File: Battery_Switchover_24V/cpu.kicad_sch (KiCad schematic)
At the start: 39 parts, among them J1 USB_C_Receptacle_USB2.0_14P, M1 Fan, Q1 PZT2222AT1G, SW1 SW_Push, U14 OPA2197xD, U3 LPC11U14FBD48-201, Y1 12.000MHz

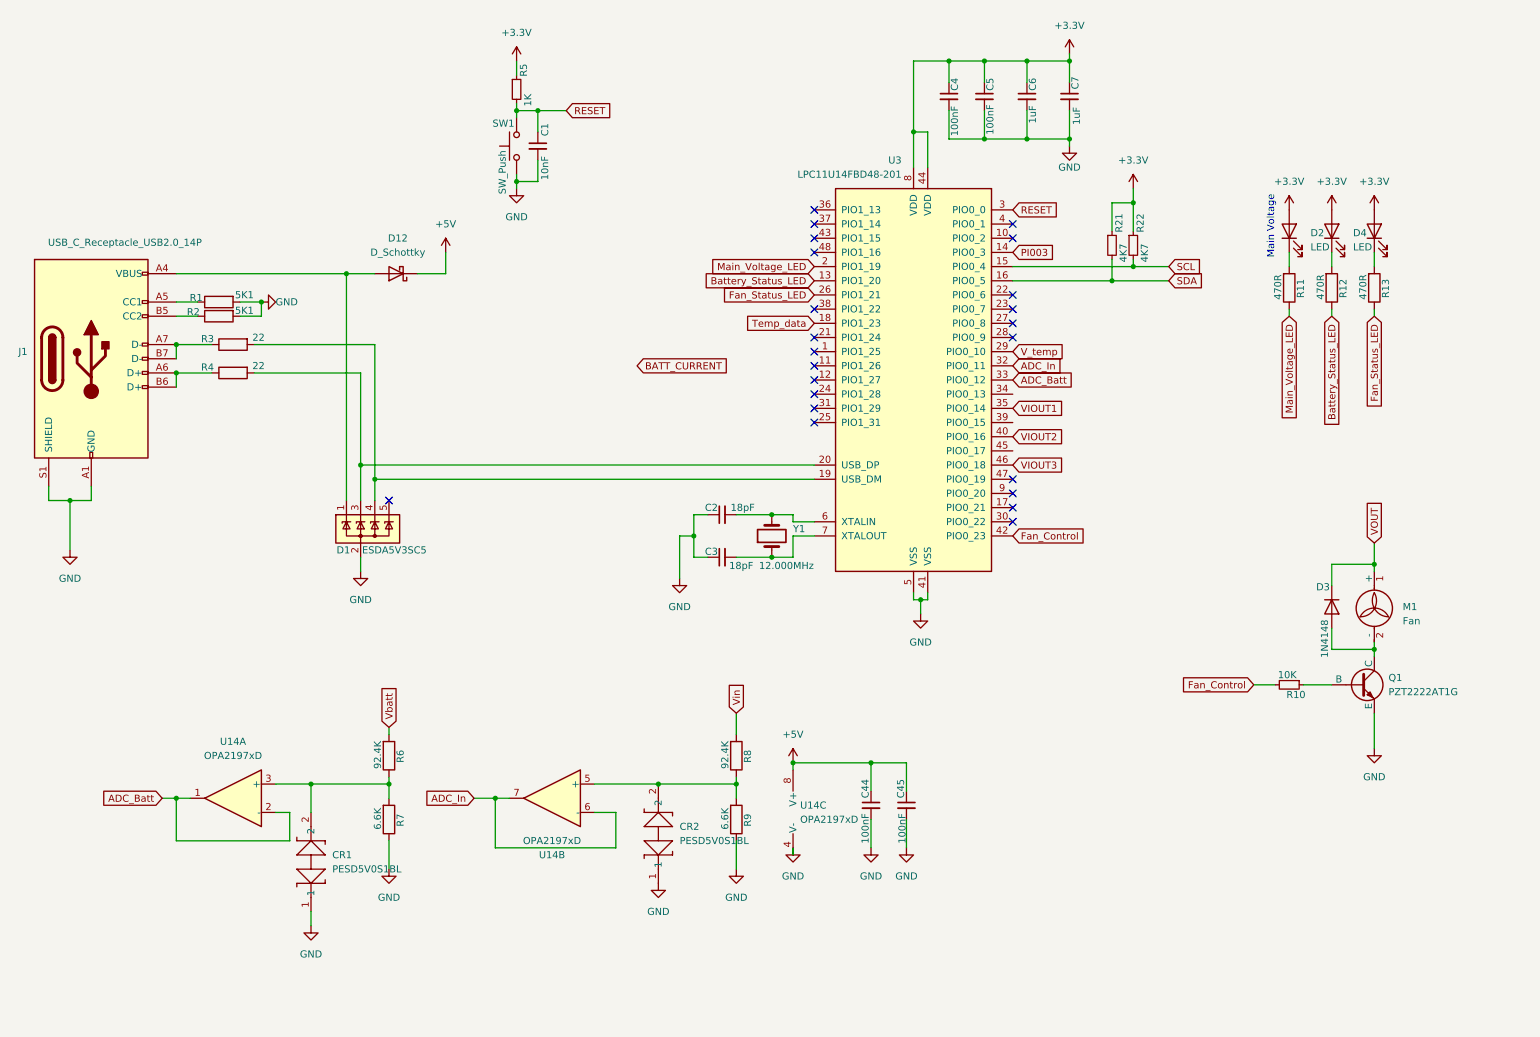
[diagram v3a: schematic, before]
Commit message: Modified labels
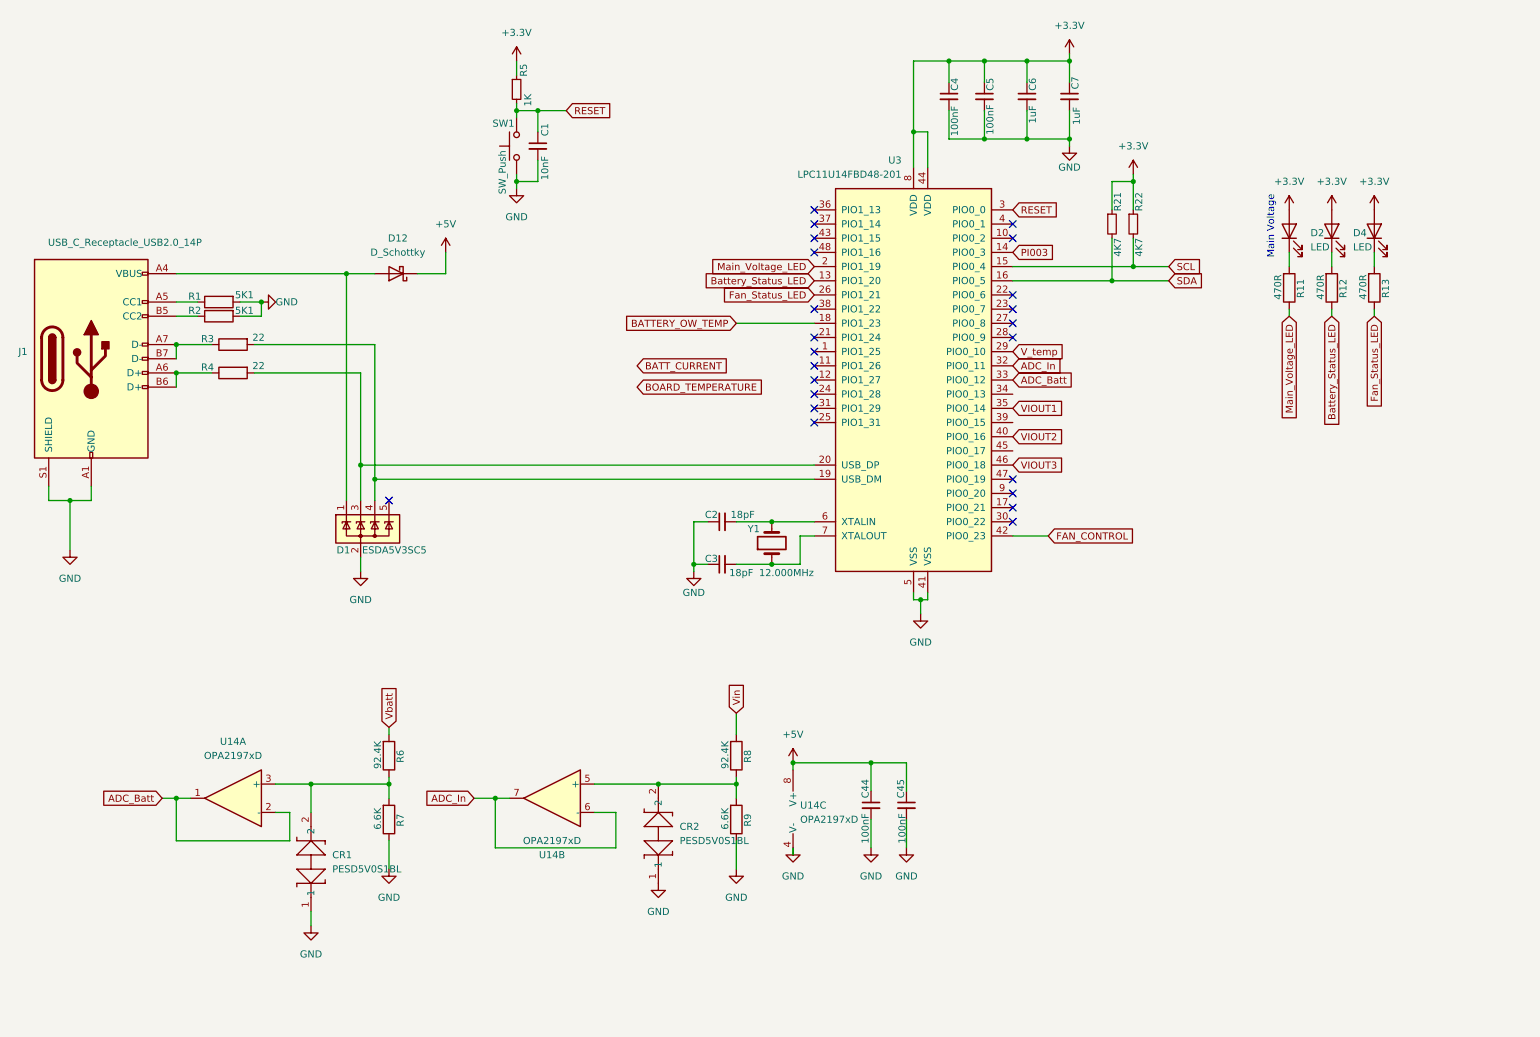
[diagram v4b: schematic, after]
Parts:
- removed D3: 1N4148, Diode_SMD:D_SMA_Handsoldering, symbol Device:D
- removed M1: Fan, TerminalBlock_Phoenix:TerminalBlock_Phoenix_PT-1,5-2-3.5-H_1x02_P3.50mm_Horizontal, symbol Motor:Fan
- removed Q1: PZT2222AT1G, Package_TO_SOT_SMD:SOT-223-3_TabPin2, symbol Simulation_SPICE:NPN
- removed R10: 10K, Resistor_SMD:R_0603_1608Metric, symbol Device:R_Small
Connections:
- net Fan_Control renamed FAN_CONTROL
- net Temp_data renamed BATTERY_OW_TEMP
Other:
- moved on the sheet: C2, C3, R21, R22, Y1

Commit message: Cm choke model and docs
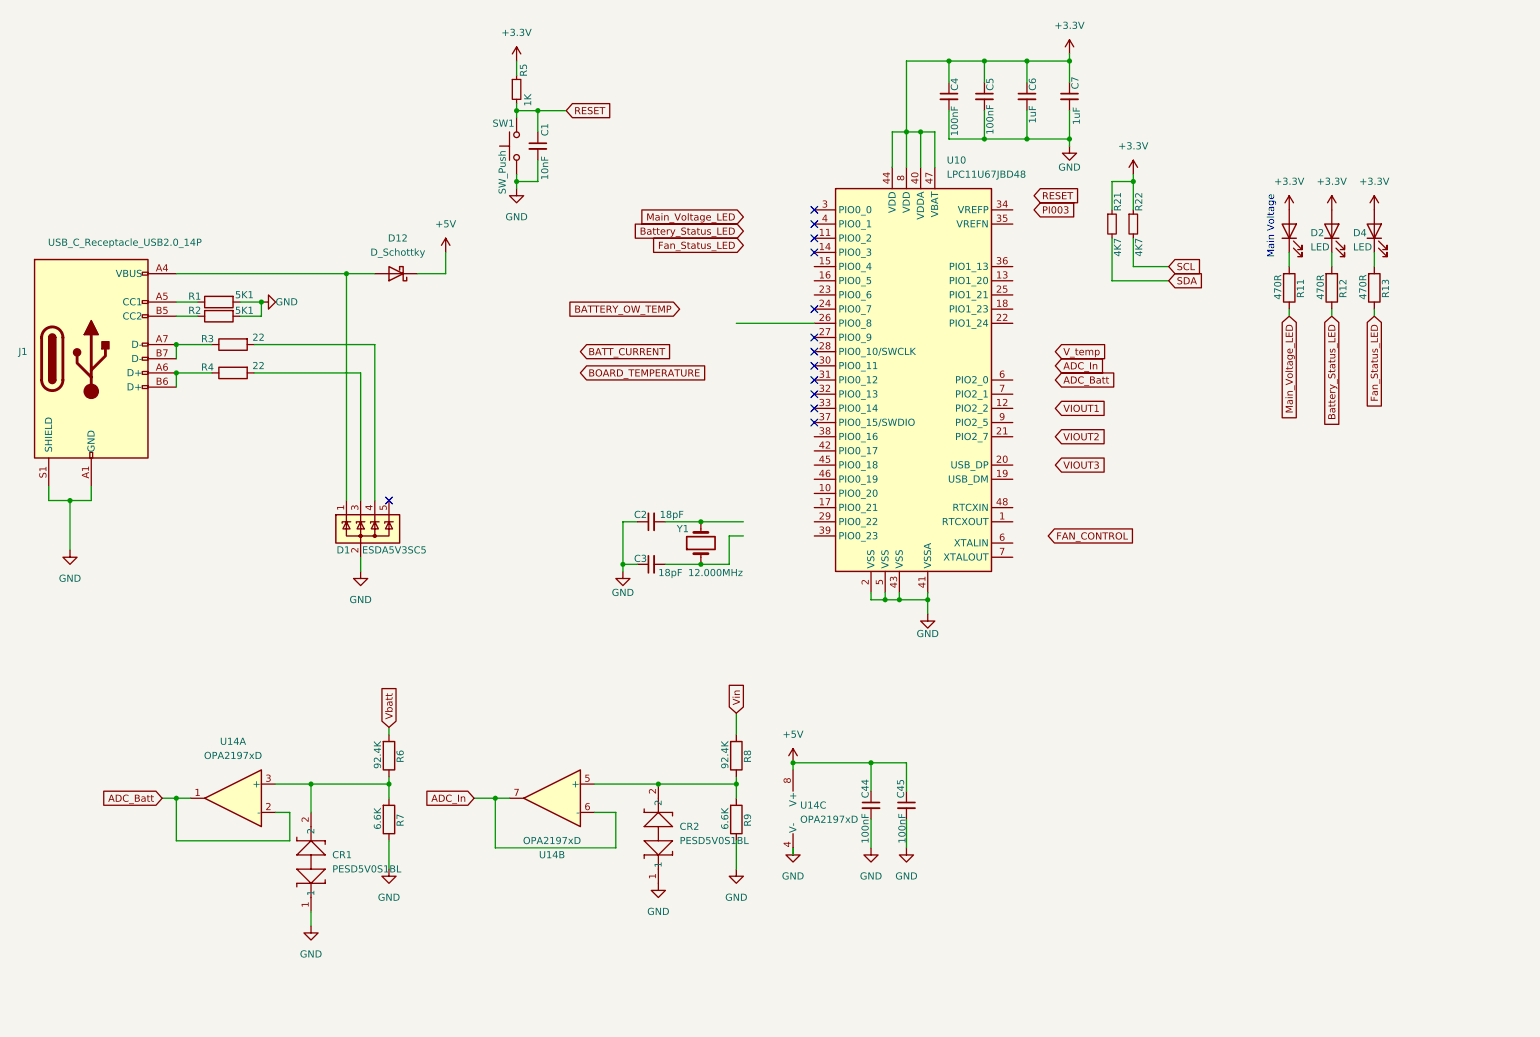
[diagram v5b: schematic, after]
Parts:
- removed U3: LPC11U14FBD48-201, Package_QFP:LQFP-48_7x7mm_P0.5mm, symbol MCU_NXP_LPC:LPC11U14FBD48-201
- added U10: LPC11U67JBD48, Package_QFP:LQFP-48_7x7mm_P0.5mm, symbol MCU_NXP_Stock:LPC11U67JBD48
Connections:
- net +3.3V: now also U10.40 (VDDA), U10.44 (VDD), U10.47 (VBAT), U10.8 (VDD)
- net GND: now also U10.2 (VSS), U10.41 (VSSA), U10.43 (VSS), U10.5 (VSS)
- no-connect marks 23 -> 13
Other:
- moved on the sheet: C2, C3, Y1

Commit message: Added load switches
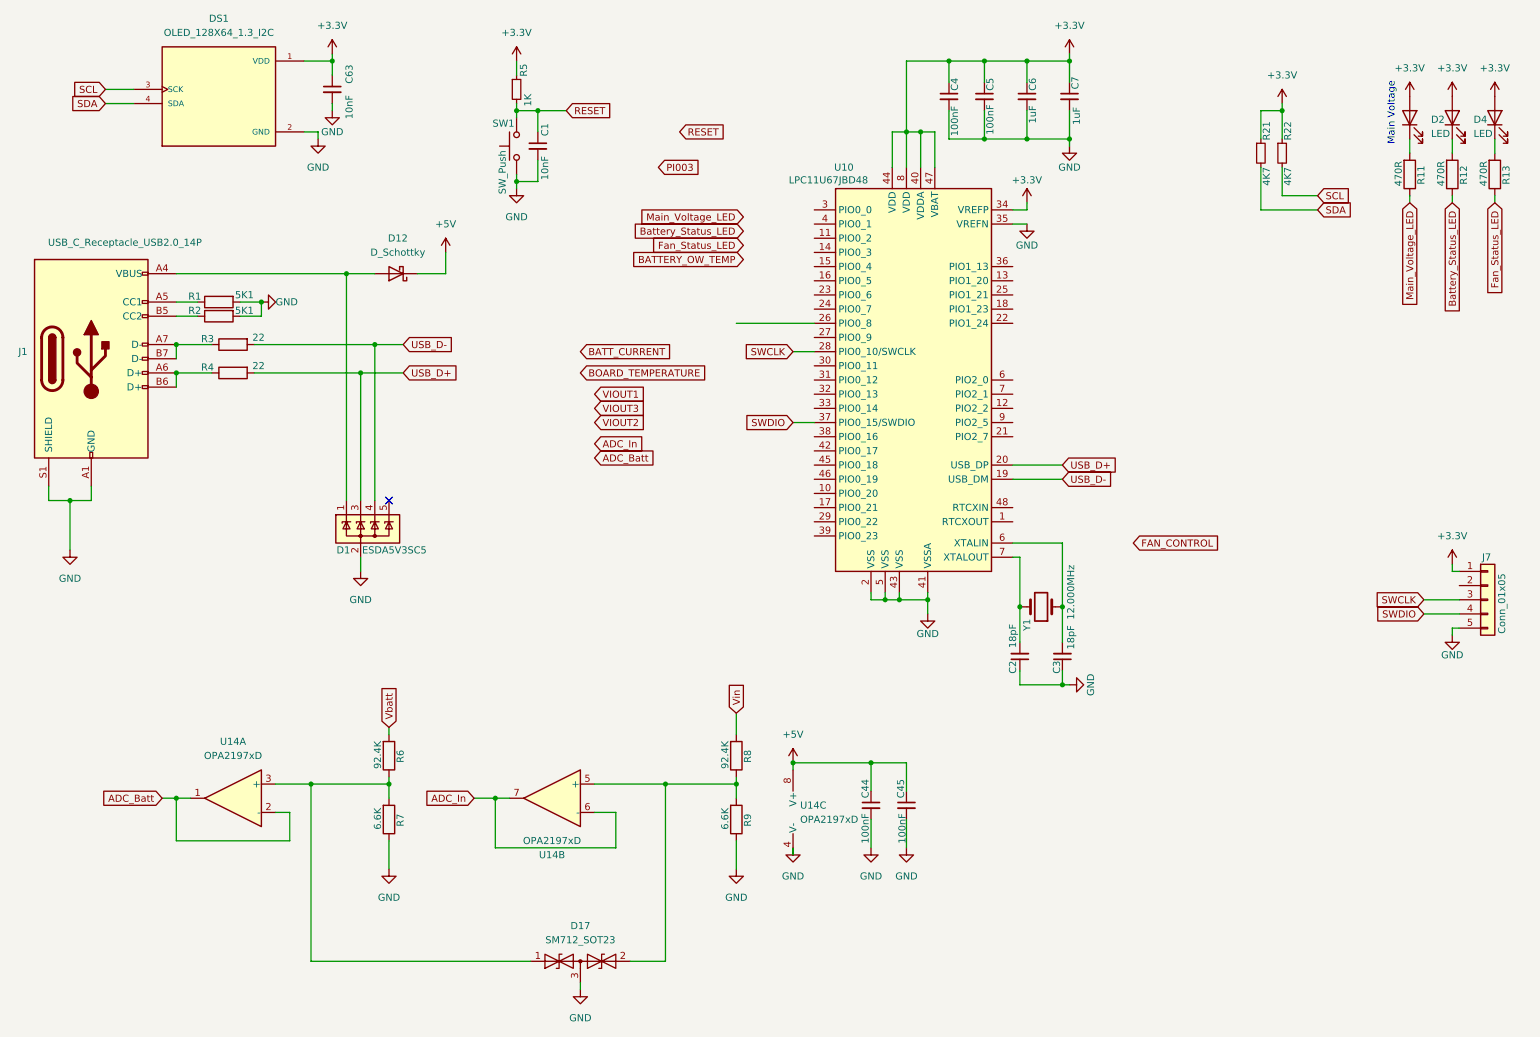
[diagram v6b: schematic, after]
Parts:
- removed CR1, CR2: PESD5V0S1BL, SOD882_NXP, symbol PESD5V0S1BL:PESD5V0S1BL
- added C63: 10nF, Capacitor_SMD:C_0603_1608Metric, symbol Device:C_Small
- added D17: SM712_SOT23, Package_TO_SOT_SMD:SOT-23, symbol Diode:SM712_SOT23
- added DS1: OLED_128X64_1.3_I2C, LCD_OLED_I2C:LCD_OLED_128X64_1.3_I2C, symbol OLED_128X64_1.3_I2C:OLED_128X64_1.3_I2C
- added J7: Conn_01x05, Connector_PinHeader_2.54mm:PinHeader_1x05_P2.54mm_Vertical, symbol Connector_Generic:Conn_01x05
- J1: footprint Connector_USB:USB_C_Receptacle_G-Switch_GT-USB-7051x -> USB_C_Vertical:GCT_USB4145-03-0170-C_REVA2
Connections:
- net +3.3V: now also U10.34 (VREFP), C63.1, DS1.1 (VDD), J7.1 (Pin_1)
- net GND: now also U10.35 (VREFN), C63.2, D17.3 (common), DS1.2 (GND), J7.5 (Pin_5)
- net SCL: now also DS1.3 (SCK)
- net SDA: now also DS1.4 (SDA)
- net at R8.1, R9.2, U14.5 (+): now also D17.2 (A2)
- net at C2.2, Y1.2: now also U10.7 (XTALOUT)
- net USB_D+: now reaches D1.3 (K), R4.2
- net USB_D+: now also U10.20 (USB_DP)
- net USB_D-: now reaches U10.19 (USB_DM)
- net USB_D-: now also D1.4 (K), R3.2
- net SWCLK: now reaches U10.28 (PIO0_10/SWCLK)
- net SWCLK: now also J7.3 (Pin_3)
- net SWDIO: now reaches U10.37 (PIO0_15/SWDIO)
- net SWDIO: now also J7.4 (Pin_4)
- net at U10.6 (XTALIN): now also C3.2, Y1.1
- net at R6.1, R7.2, U14.3 (+): now also D17.1 (A1)
- no-connect marks 13 -> 1
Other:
- moved on the sheet: C2, C3, D2, D4, R11, R12, R13, R21, R22, Y1

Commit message: adc pins holes
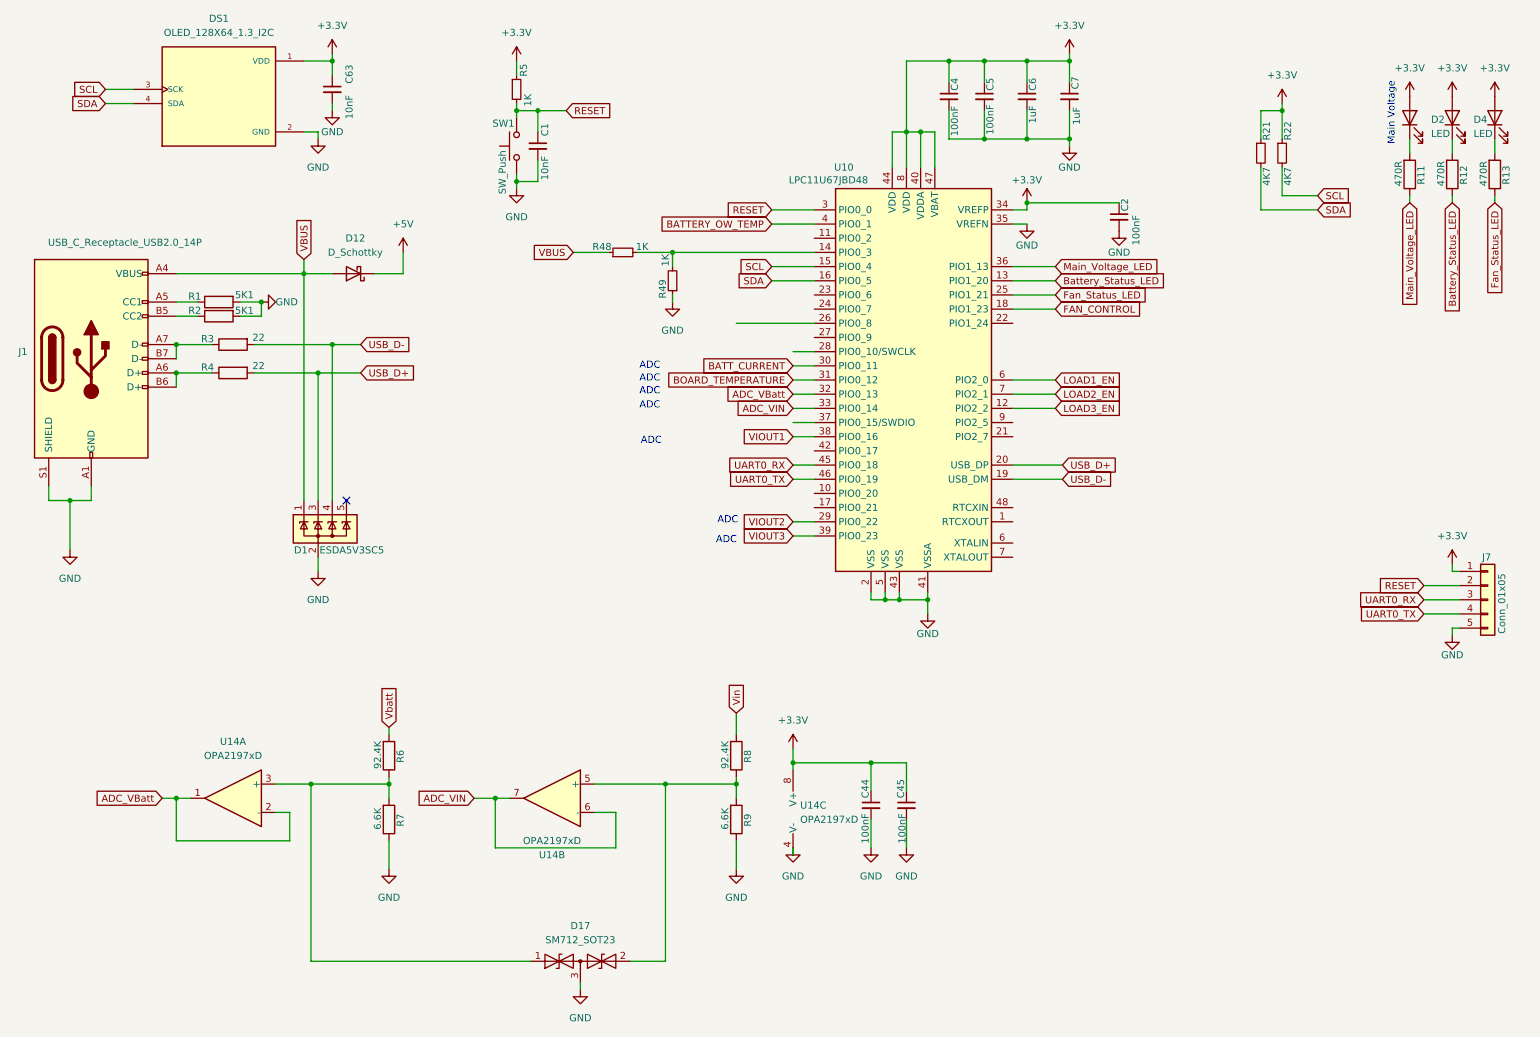
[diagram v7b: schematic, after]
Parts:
- removed C3: 18pF, Capacitor_SMD:C_0402_1005Metric, symbol Device:C_Small
- removed Y1: 12.000MHz, Crystal:Crystal_SMD_TXC_7M-4Pin_3.2x2.5mm, symbol Device:Crystal
- added R48, R49: 1K, Resistor_SMD:R_0603_1608Metric, symbol Device:R_Small
- C2: value 18pF -> 100nF; footprint Capacitor_SMD:C_0402_1005Metric -> Capacitor_SMD:C_0603_1608Metric
- D12: footprint (none) -> Diode_SMD:D_SOD-323_HandSoldering
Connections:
- net ADC_Batt is gone; now on net ADC_VBatt: U14.1, U14.2 (-)
- net ADC_In is gone; now on net ADC_VIN: U14.6 (-), U14.7
- net +3.3V: now also C2.1, C44.1, C45.1, U14.8 (V+)
- net +5V: no longer C44.1, C45.1, U14.8 (V+)
- net BATTERY_OW_TEMP: now also U10.4 (PIO0_1)
- net BATT_CURRENT: now also U10.30 (PIO0_11)
- net BOARD_TEMPERATURE: now also U10.31 (PIO0_12)
- net Battery_Status_LED: now also U10.13 (PIO1_20)
- net FAN_CONTROL: now also U10.18 (PIO1_23)
- net Fan_Status_LED: now also U10.25 (PIO1_21)
- net GND: now also C2.2, R49.1; no longer C2.1
- net Main_Voltage_LED: now also U10.36 (PIO1_13)
- net RESET: now also J7.2 (Pin_2), U10.3 (PIO0_0)
- net SCL: now also U10.15 (PIO0_4)
- net SDA: now also U10.16 (PIO0_5)
- net VIOUT1: now also U10.38 (PIO0_16)
- net VIOUT2: now also U10.29 (PIO0_22)
- net VIOUT3: now also U10.39 (PIO0_23)
- net LOAD2_EN: now reaches U10.7 (XTALOUT)
- net LOAD2_EN: no longer C2.2
- net LOAD3_EN: now reaches U10.12 (PIO2_2)
- net at U10.14 (PIO0_3): now also R48.2, R49.2
- net ADC_VBatt: now reaches U10.32 (PIO0_13)
- net ADC_VIN: now reaches U10.33 (PIO0_14)
- net UART0_RX: now reaches U10.45 (PIO0_18)
- net UART0_RX: now also J7.3 (Pin_3)
- net UART0_TX: now reaches U10.46 (PIO0_19)
- net UART0_TX: now also J7.4 (Pin_4)
- net LOAD1_EN: now reaches U10.6 (XTALIN)
- net VBUS: now reaches D1.1 (K), D12.2 (A), J1.A4 (VBUS), J1.A9 (VBUS), J1.B4 (VBUS), J1.B9 (VBUS)
- net VBUS: now also R48.1
- net SWCLK: no longer names the net of U10.28 (PIO0_10/SWCLK)
- net SWCLK: no longer J7.3 (Pin_3)
- net SWDIO: no longer names the net of U10.37 (PIO0_15/SWDIO)
- net SWDIO: no longer J7.4 (Pin_4)
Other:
- note added: "ADC"
- moved on the sheet: D1, D12
